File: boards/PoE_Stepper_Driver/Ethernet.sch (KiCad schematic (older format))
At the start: 20 parts, among them J1 RJ45_Shielded, U1 LT4321, U2 LT4293

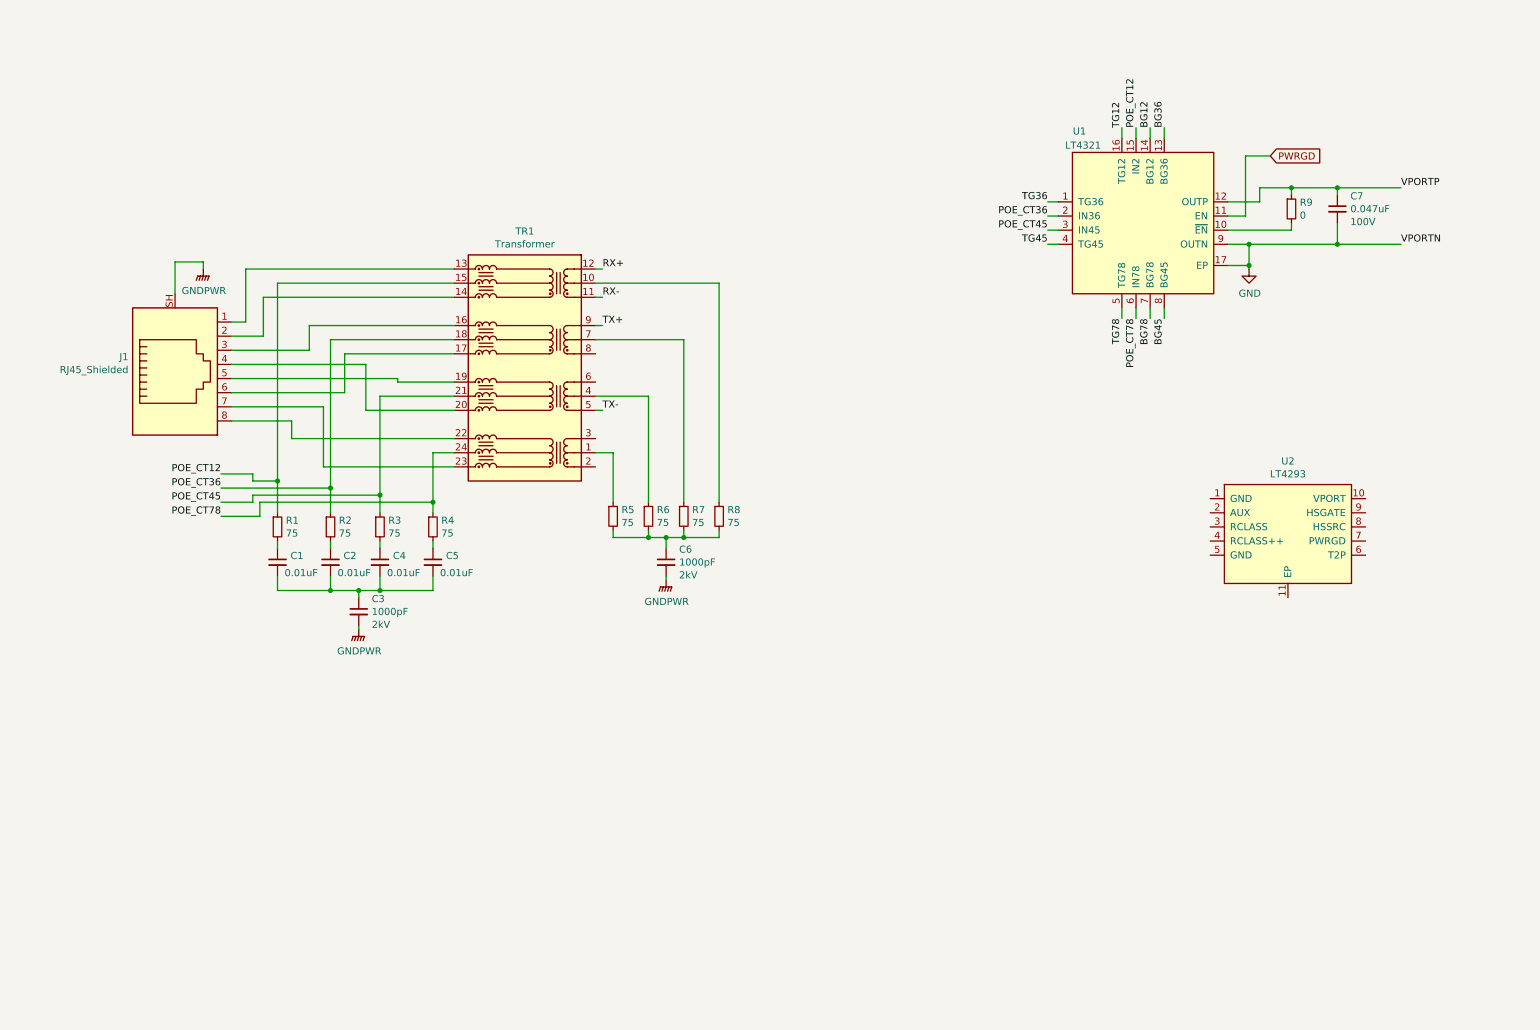
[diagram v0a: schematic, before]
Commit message: almost done with ethernet schematic, need phy and annotations
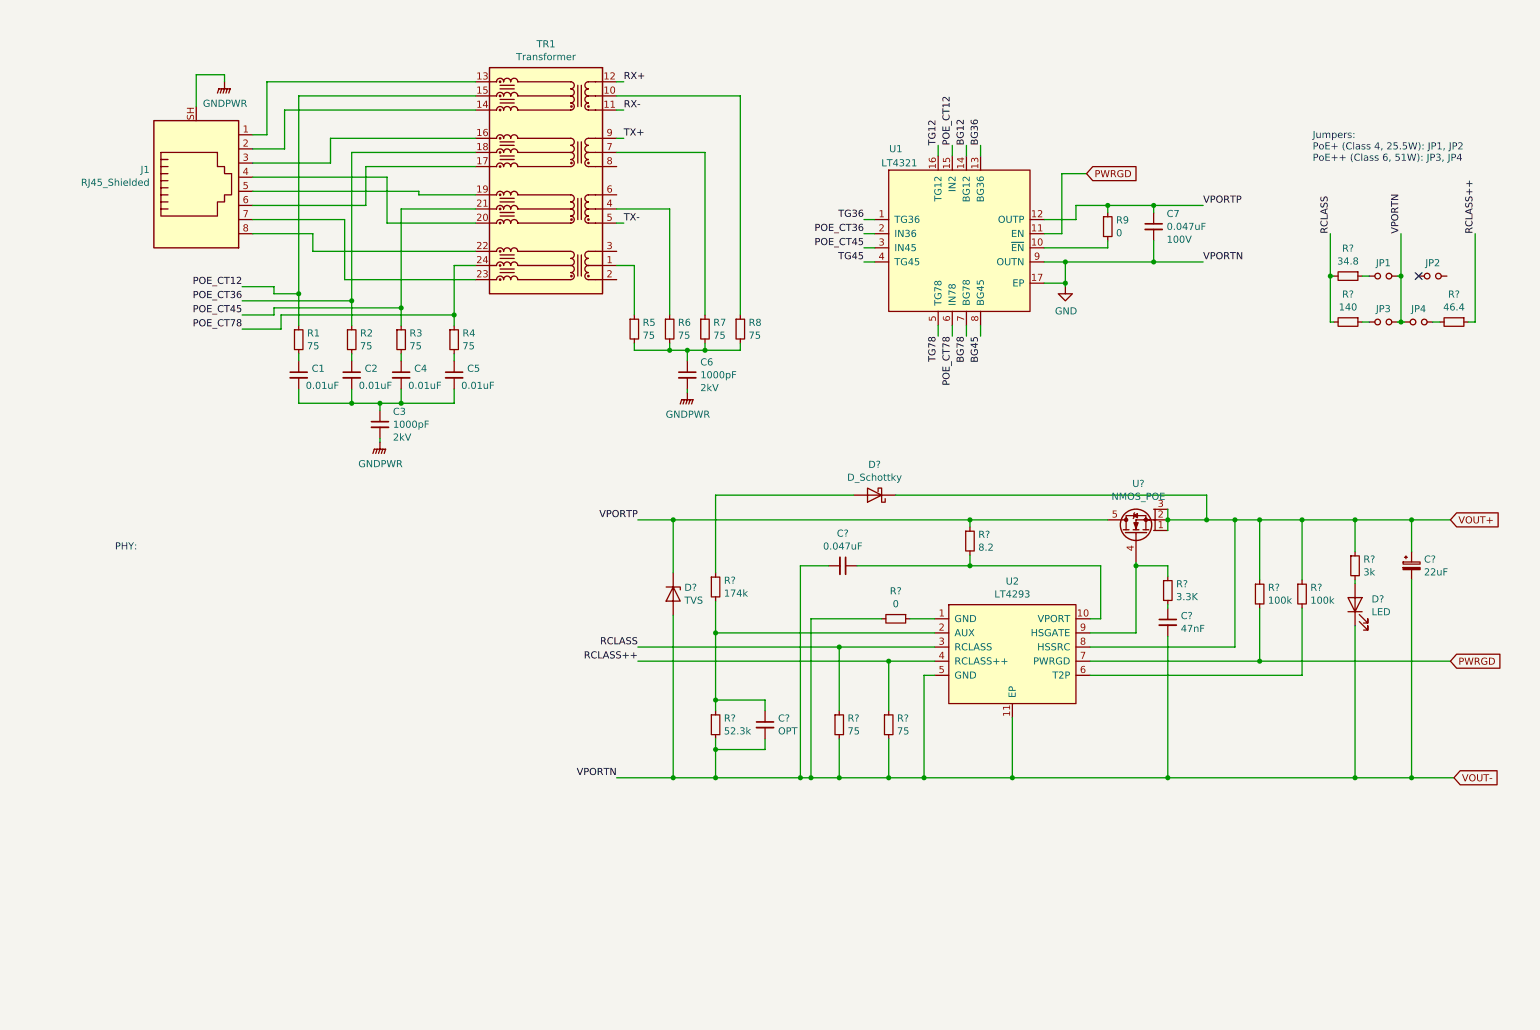
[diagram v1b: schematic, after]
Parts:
- added C?: 0.047uF, symbol device:C_Small
- added C?: 47nF, symbol device:C_Small
- added C?: OPT, symbol device:C_Small
- added C?: 22uF, symbol device:CP_Small
- added D?: D_Schottky, symbol device:D_Schottky
- added D?: TVS, symbol device:D_Zener
- added D?: LED, symbol device:LED
- added JP1, JP2, JP3, JP4: Jumper_NO_Small, symbol device:Jumper_NO_Small
- added R?: 174k, symbol device:R_Small
- added R?: 8.2, symbol device:R_Small
- added R? (x2): 75, symbol device:R_Small
- added R?: 3.3K, symbol device:R_Small
- added R?: 0, symbol device:R_Small
- added R?: 52.3k, symbol device:R_Small
- added R? (x2): 100k, symbol device:R_Small
- added R?: 3k, symbol device:R_Small
- added R?: 34.8, symbol device:R_Small
- added R?: 140, symbol device:R_Small
- added R?: 46.4, symbol device:R_Small
- added U?: NMOS_POE, symbol ECE445:NMOS_POE
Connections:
- net GND: now also U2.11 (EP), U2.5 (GND), C?.2, C?.2, C?.2, C?.2, D?.1 (K), D?.2 (A), JP1.2, JP3.2, JP4.1, R?.2, R?.2, R?.2, R?.2
- net PWRGD: now also U2.7 (PWRGD), R?.2
- net VPORTP: now also D?.1 (K), R?.1, U?.5
- net at U2.1 (GND): now also R?.1
- net at U2.10 (VPORT): now also C?.1, R?.2
- net at U2.2 (AUX): now also C?.1, R?.1, R?.2
- net RCLASS: now reaches U2.3 (RCLASS)
- net RCLASS: now also R?.1, R?.2, R?.2
- net RCLASS++: now reaches U2.4 (RCLASS++)
- net RCLASS++: now also R?.1, R?.1
- net at U2.6 (T2P): now also R?.2
- net VOUT+: now reaches U2.8 (HSSRC)
- net VOUT+: now also C?.1, D?.1 (K), R?.1, R?.1, R?.1, U?.1, U?.2, U?.3
- net at U2.9 (HSGATE): now also R?.1, U?.4
- new net: D?.2 (A), R?.1
- new net: C?.1, R?.2
- new net: D?.2 (A), R?.2
- new net: JP1.1, R?.1
- new net: JP3.1, R?.1
- new net: JP4.2, R?.2
- no-connect marks 0 -> 1
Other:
- note added: "Jumpers:\nPoE+ (Class 4, 25.5W): JP1, JP2\nPoE++ (Class 6, 51W): JP3, JP4"
- note added: "PHY:"
- moved on the sheet: C1, C2, C3, C4, C5, C6, C7, J1, R1, R2, R3, R4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

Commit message: added trinamic chips
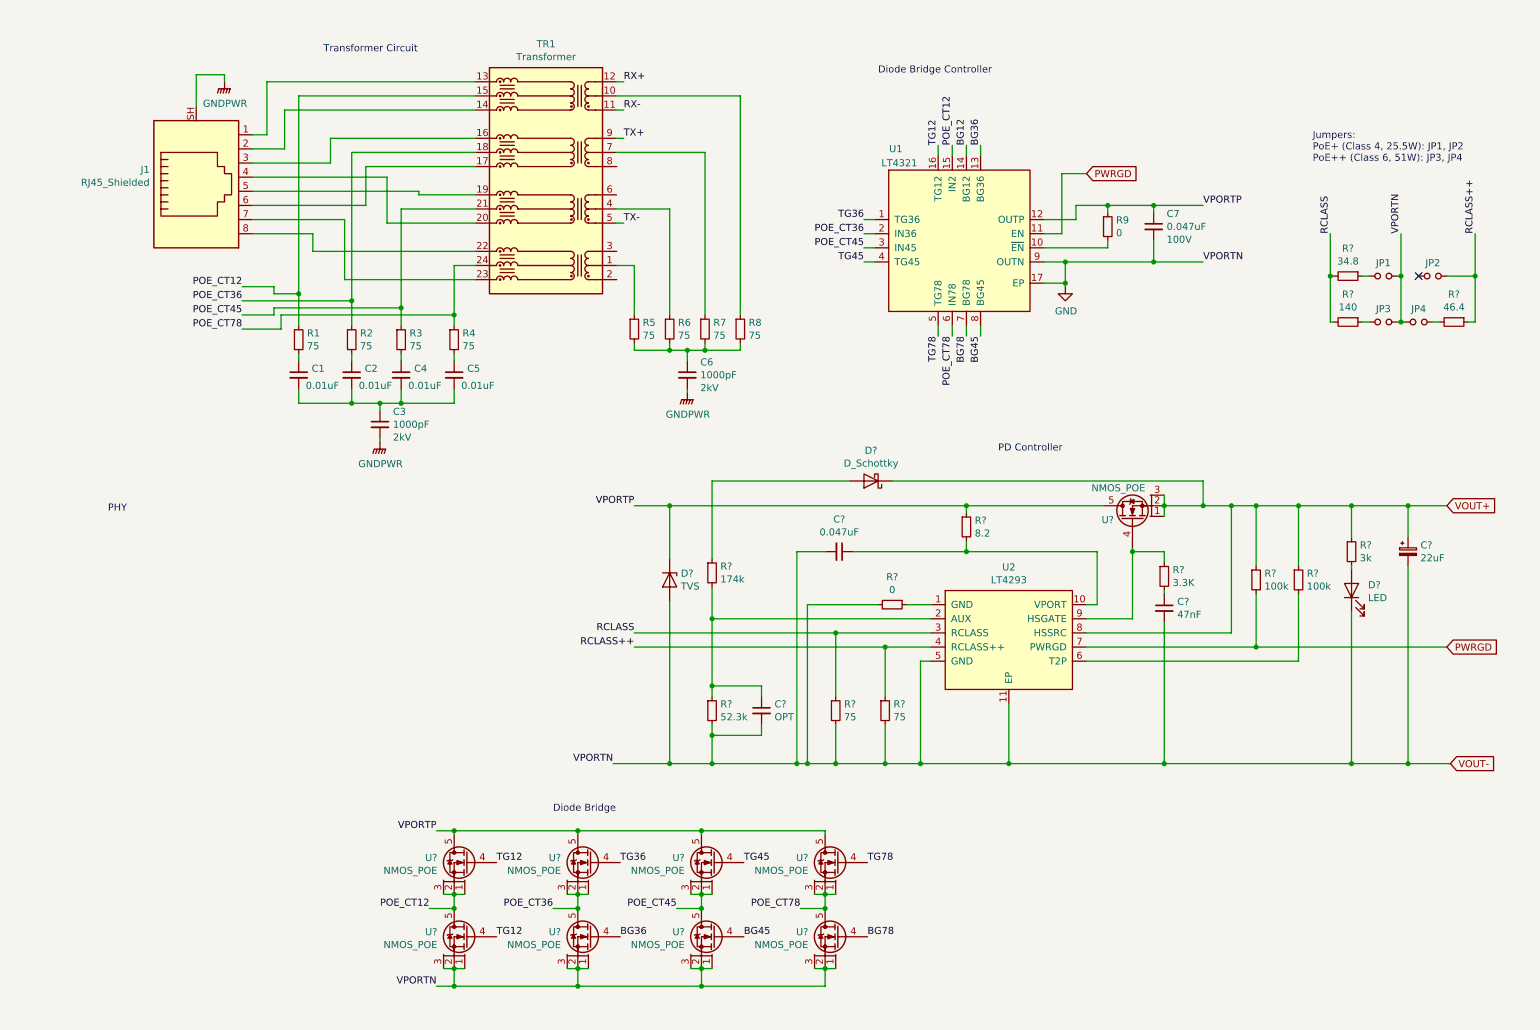
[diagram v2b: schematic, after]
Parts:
- added U? (x8): NMOS_POE, symbol ECE445:NMOS_POE
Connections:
- net BG36: now also U?.4
- net BG45: now also U?.4
- net BG78: now also U?.4
- net GND: now also U?.1, U?.1, U?.1, U?.1, U?.2, U?.2, U?.2, U?.2, U?.3, U?.3, U?.3, U?.3
- net POE_CT12: now also U?.1, U?.2, U?.3, U?.5
- net POE_CT36: now also U?.1, U?.2, U?.3, U?.5
- net POE_CT45: now also U?.1, U?.2, U?.3, U?.5
- net POE_CT78: now also U?.1, U?.2, U?.3, U?.5
- net RCLASS++: now also JP2.2
- net TG12: now also U?.4, U?.4
- net TG36: now also U?.4
- net TG45: now also U?.4
- net TG78: now also U?.4
- net VPORTP: now also U?.5, U?.5, U?.5, U?.5
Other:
- note added: "Diode Bridge"
- note added: "Diode Bridge Controller"
- note added: "PD Controller"
- note added: "PHY"
- note added: "Transformer Circuit"
- note removed: "PHY:"
- moved on the sheet: C?, D?, R?, U2, U?

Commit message: added phy schematic symbol
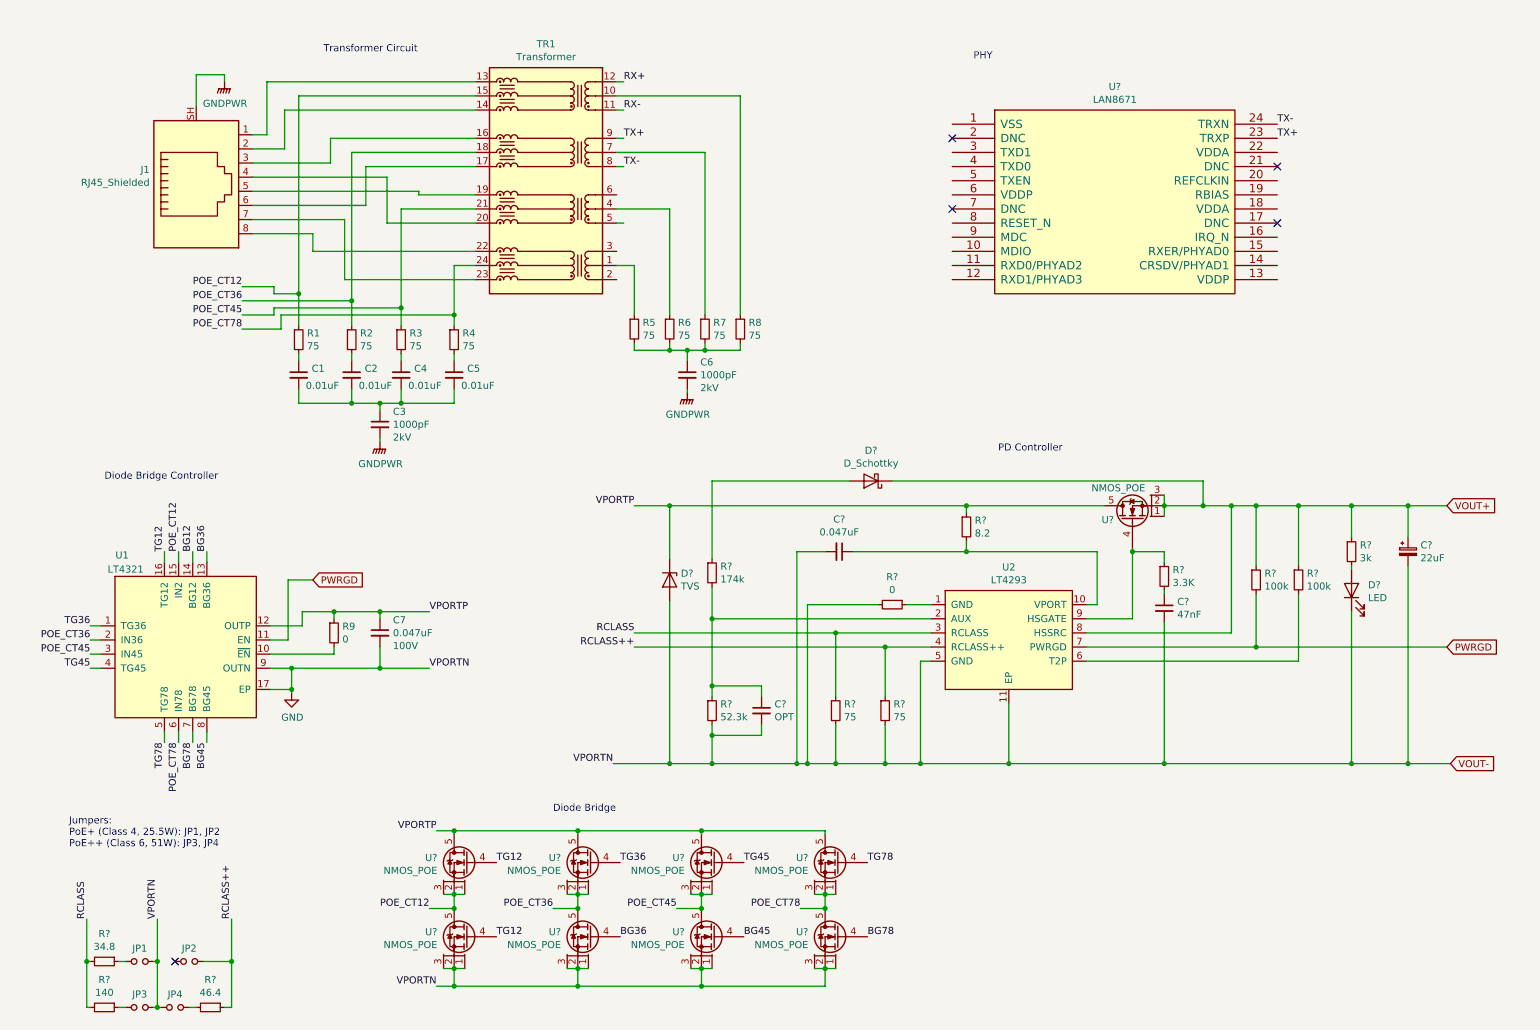
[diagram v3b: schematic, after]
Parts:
- added U?: LAN8671, symbol ECE445:LAN8671
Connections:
- net TX+: now also U?.23 (TRXP)
- net TX-: now also TR1.8 (TD3+), U?.24 (TRXN); no longer TR1.5 (TD2+)
- no-connect marks 1 -> 5
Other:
- moved on the sheet: C7, JP1, JP2, JP3, JP4, R9, R?, U1

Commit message: added actual phy
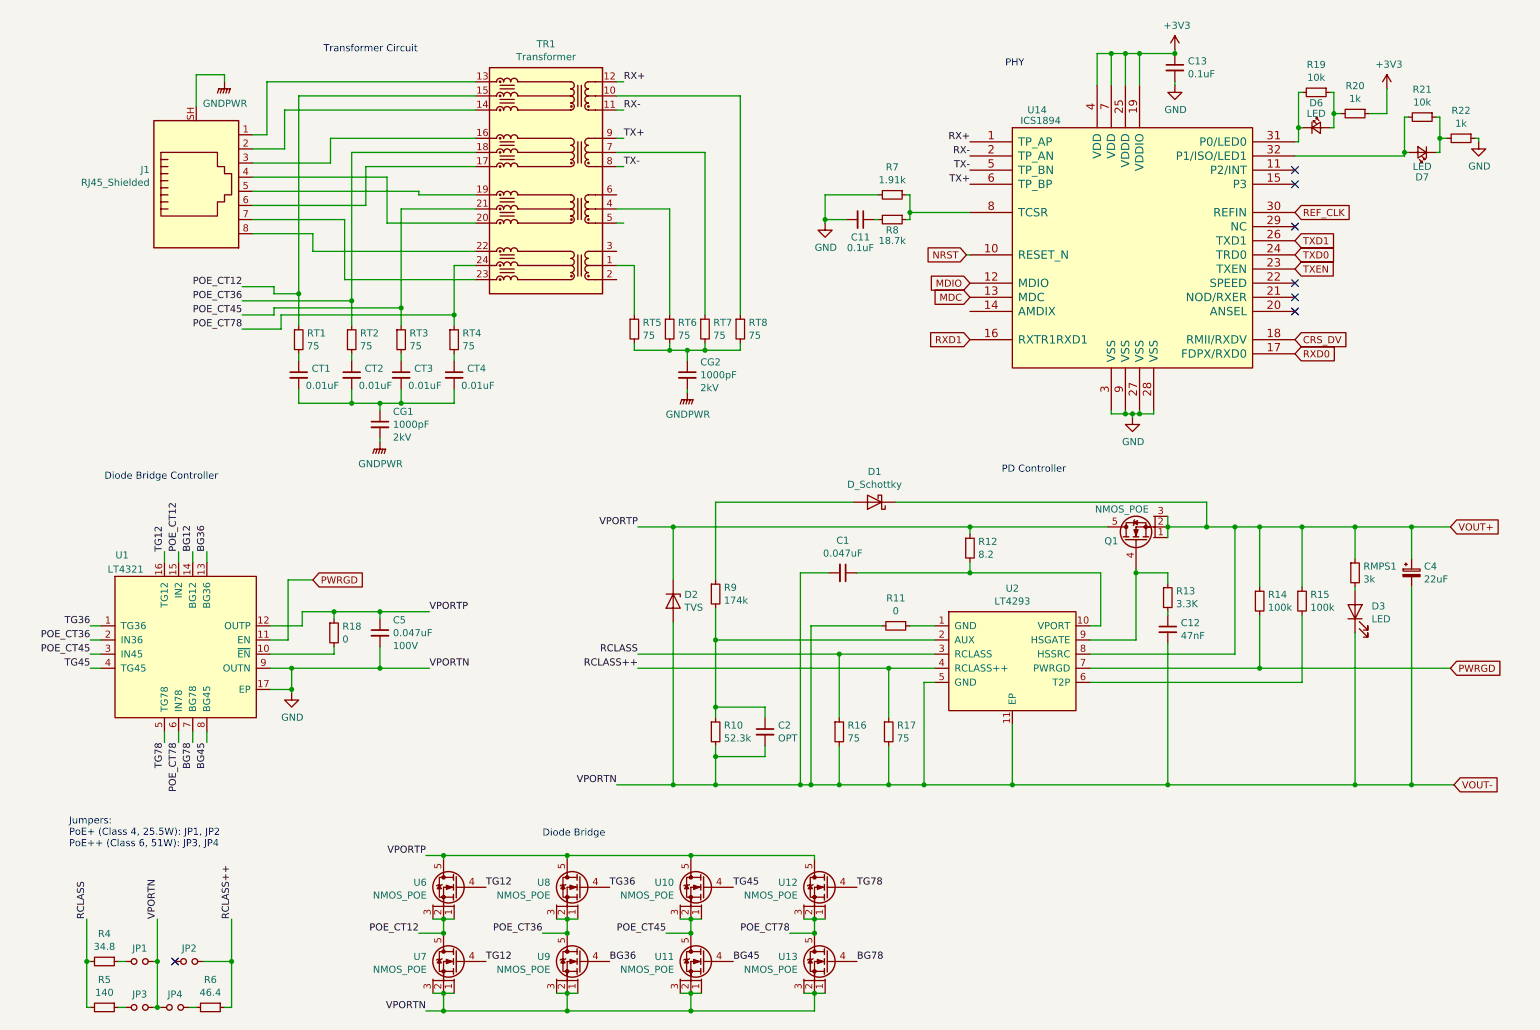
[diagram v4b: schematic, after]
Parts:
- removed U?: LAN8671, symbol ECE445:LAN8671
- added C11, C13: 0.1uF, symbol device:C_Small
- added D6, D7: LED, symbol device:LED_Small
- added R19, R21: 10k, symbol device:R_Small
- added R20, R22: 1k, symbol device:R_Small
- added R7: 1.91k, symbol device:R_Small
- added R8: 18.7k, symbol device:R_Small
- added U14: ICS1894, symbol ECE445:ICS1894
- gave numbers to parts that had none: 29
- renumbered C7 to C5, C3 to CG1, C6 to CG2, C1 to CT1, C2 to CT2, C4 to CT3, C5 to CT4, R9 to R18, R1 to RT1, R2 to RT2, R3 to RT3, R4 to RT4, R5 to RT5, R6 to RT6, R7 to RT7, R8 to RT8
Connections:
- net GND: now also C11.2, C13.2, R22.1, R7.2, U14.27 (VSS), U14.28 (VSS), U14.3 (VSS), U14.9 (VSS)
- net RX+: now also U14.1 (TP_AP)
- net RX-: now also U14.2 (TP_AN)
- net TX+: now also U14.6 (TP_BP)
- net TX-: now also U14.5 (TP_BN)
- new net: D6.1 (K), R19.2, U14.31 (P0/LED0)
- new net: D7.2 (A), R21.2, U14.32 (P1/ISO/LED1)
- new net: R7.1, R8.1, U14.8 (TCSR)
- new net: D6.2 (A), R19.1, R20.2
- new net: D7.1 (K), R21.1, R22.2
- new net: C11.1, R8.2
- new net +3V3: C13.1, R20.1, U14.19 (VDDIO), U14.25 (VDDD), U14.4 (VDD), U14.7 (VDD)
- new net CRS_DV: U14.18 (RMII/RXDV)
- new net MDC: U14.13 (MDC)
- new net MDIO: U14.12 (MDIO)
- new net NRST: U14.10 (RESET_N)
- new net REF_CLK: U14.30 (REFIN)
- new net RXD0: U14.17 (FDPX/RXD0)
- new net RXD1: U14.16 (RXTR1RXD1)
- new net TXD0: U14.24 (TRD0)
- new net TXD1: U14.26 (TXD1)
- new net TXEN: U14.23 (TXEN)
- no-connect marks 5 -> 7
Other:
- moved on the sheet: C1, C12, C2, C4, D1, D2, D3, Q1, R10, R11, R12, R13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
